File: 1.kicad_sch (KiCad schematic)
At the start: 32 parts, among them IC1 LTC4361IDC-2#TRMPBF, IC2 SI1470DH-T1-E3, IC3 SI1470DH-T1-E3, IC4 LTC4361IDC-2#TRMPBF, J1 Screw_Terminal_01x03, J2 Screw_Terminal_01x01, J3 Screw_Terminal_01x01, J4 ON2, J5 ON1, U1 LTC2990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

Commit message: Patch
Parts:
- removed IC1, IC4: LTC4361IDC-2#TRMPBF, SON45P200X200X80-9N-D, symbol LTC4361IDC-2#TRMPBF:LTC4361IDC-2#TRMPBF
- removed IC2, IC3: SI1470DH-T1-E3, SOT65P210X110-6N, symbol SI1470DH-T1-E3:SI1470DH-T1-E3
- removed J4: ON2, Connector_PinHeader_1.00mm:PinHeader_1x01_P1.00mm_Vertical, symbol Connector:Conn_01x01_Male
- removed J5: ON1, Connector_PinHeader_1.00mm:PinHeader_1x01_P1.00mm_Vertical, symbol Connector:Conn_01x01_Male
- removed R3, R4: 0.025, 0.025 ohm rst:CRA2512-FZ-R025ELF, symbol Device:R
- R5, R6, R7: value 60m -> 50m; footprint 60 mil rst:RESC7146X175N -> 50m RST:RESC3216X88N
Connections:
- net at R6.1, U2.1 (V1), U2.10 (VCC): now also Buck_IC1.4 (FB), C4.1, L2.2
- net at Boost_IC1.5 (VOUT), C2.2, D1.1 (K)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: now also R7.1, U3.1 (V1), U3.10 (VCC)
- no-connect marks 2 -> 0
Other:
- moved on the sheet: J1, R6, R7, SCLSDA1, SCLSDA2, U2, U3

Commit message: Fix
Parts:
- removed SHDN1: EN, Connector_PinHeader_1.00mm:PinHeader_1x02_P1.00mm_Vertical, symbol Connector:Conn_01x02_Male
- added R3: 1M, 1MEGA RST:RESC1608X55N, symbol Device:R
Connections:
- net at Boost_IC1.1 (SW), Buck_IC1.1 (VI), C1.1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: now also Buck_IC1.3 (EN)
- net at Boost_IC1.6 (VIN), D1.2 (A), L1.2: now also R3.2
- net at Boost_IC1.4 (~{SHDN}): now also R3.1
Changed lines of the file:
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@@
   (junction (at 129.54 83.82) (diameter 0) (color 0 0 0 0)
   )
+  (junction (at 110.49 110.49) (diameter 0) (color 0 0 0 0)
+  )
   (junction (at 162.56 120.65) (diameter 0) (color 0 0 0 0)
   )
@@
   (junction (at 162.56 125.73) (diameter 0) (color 0 0 0 0)
   )
+  (junction (at 76.2 83.82) (diameter 0) (color 0 0 0 0)
+  )
   (junction (at 162.56 33.02) (diameter 0) (color 0 0 0 0)
   )
@@
     (stroke (width 0) (type default) (color 0 0 0 0))
   )
+  (wire (pts (xy 110.49 110.49) (xy 110.49 105.41))
+    (stroke (width 0) (type default) (color 0 0 0 0))
+  )
   (wire (pts (xy 53.34 83.82) (xy 57.15 83.82))
     (stroke (width 0) (type default) (color 0 0 0 0))
@@
     (stroke (width 0) (type default) (color 0 0 0 0))
   )
-  (wire (pts (xy 53.34 109.22) (xy 53.34 105.41))
-    (stroke (width 0) (type default) (color 0 0 0 0))
-  )
   (wire (pts (xy 46.99 39.37) (xy 48.26 39.37))
     (stroke (width 0) (type default) (color 0 0 0 0))
@@
     (stroke (width 0) (type default) (color 0 0 0 0))
   )
+  (wire (pts (xy 76.2 83.82) (xy 76.2 100.33))
+    (stroke (width 0) (type default) (color 0 0 0 0))
+  )
   (wire (pts (xy 77.47 114.3) (xy 77.47 119.38))
     (stroke (width 0) (type default) (color 0 0 0 0))
@@
     (stroke (width 0) (type default) (color 0 0 0 0))
   )
+  (wire (pts (xy 116.84 118.11) (xy 116.84 110.49))
+    (stroke (width 0) (type default) (color 0 0 0 0))
+  )
   (wire (pts (xy 121.92 105.41) (xy 124.46 105.41))
     (stroke (width 0) (type default) (color 0 0 0 0))
   )
-  (wire (pts (xy 66.04 83.82) (xy 85.09 83.82))
+  (wire (pts (xy 66.04 83.82) (xy 76.2 83.82))
     (stroke (width 0) (type default) (color 0 0 0 0))
   )
@@
     (stroke (width 0) (type default) (color 0 0 0 0))
   )
-  (wire (pts (xy 53.34 100.33) (xy 53.34 102.87))
-    (stroke (width 0) (type default) (color 0 0 0 0))
-  )
   (wire (pts (xy 54.61 44.45) (xy 60.96 44.45))
     (stroke (width 0) (type default) (color 0 0 0 0))
@@
     (stroke (width 0) (type default) (color 0 0 0 0))
   )
+  (wire (pts (xy 76.2 83.82) (xy 85.09 83.82))
+    (stroke (width 0) (type default) (color 0 0 0 0))
+  )
   (wire (pts (xy 163.83 39.37) (xy 163.83 33.02))
     (stroke (width 0) (type default) (color 0 0 0 0))
@@
     (stroke (width 0) (type default) (color 0 0 0 0))
   )
-  (wire (pts (xy 110.49 111.76) (xy 110.49 105.41))
+  (wire (pts (xy 110.49 111.76) (xy 110.49 110.49))
     (stroke (width 0) (type default) (color 0 0 0 0))
   )
@@
     (stroke (width 0) (type default) (color 0 0 0 0))
   )
+  (wire (pts (xy 85.09 100.33) (xy 76.2 100.33))
+    (stroke (width 0) (type default) (color 0 0 0 0))
+  )
   (wire (pts (xy 194.31 125.73) (xy 170.18 125.73))
     (stroke (width 0) (type default) (color 0 0 0 0))
   )
-  (wire (pts (xy 53.34 100.33) (xy 85.09 100.33))
-    (stroke (width 0) (type default) (color 0 0 0 0))
-  )
   (wire (pts (xy 57.15 83.82) (xy 66.04 83.82))
     (stroke (width 0) (type default) (color 0 0 0 0))
   )
-  (wire (pts (xy 113.03 125.73) (xy 55.88 125.73))
-    (stroke (width 0) (type default) (color 0 0 0 0))
-  )
   (wire (pts (xy 194.31 100.33) (xy 200.66 100.33))
     (stroke (width 0) (type default) (color 0 0 0 0))
@@
     (stroke (width 0) (type default) (color 0 0 0 0))
   )
+  (wire (pts (xy 113.03 125.73) (xy 116.84 125.73))
+    (stroke (width 0) (type default) (color 0 0 0 0))
+  )
   (wire (pts (xy 161.29 67.31) (xy 161.29 69.85))
     (stroke (width 0) (type default) (color 0 0 0 0))
   )
+  (wire (pts (xy 116.84 110.49) (xy 110.49 110.49))
+    (stroke (width 0) (type default) (color 0 0 0 0))
+  )
   (wire (pts (xy 137.16 114.3) (xy 124.46 114.3))
     (stroke (width 0) (type default) (color 0 0 0 0))
@@
     (stroke (width 0) (type default) (color 0 0 0 0))
   )
-  (wire (pts (xy 55.88 125.73) (xy 55.88 109.22))
-    (stroke (width 0) (type default) (color 0 0 0 0))
-  )
   (wire (pts (xy 180.34 88.9) (xy 186.69 88.9))
     (stroke (width 0) (type default) (color 0 0 0 0))
@@
   )
   (wire (pts (xy 129.54 83.82) (xy 133.35 83.82))
-    (stroke (width 0) (type default) (color 0 0 0 0))
-  )
-  (wire (pts (xy 55.88 109.22) (xy 53.34 109.22))
     (stroke (width 0) (type default) (color 0 0 0 0))
   )
@@
     (pin "1")
   )
+  (symbol (lib_id "Device:R") (at 116.84 121.92 180) (unit 1)
+    (in_bom yes) (on_board yes) (fields_autoplaced)
+    (property "Reference" "R3" (id 0) (at 119.38 120.6499 0)
+      (effects (font (size 1.27 1.27)) (justify right))
+    )
+    (property "Value" "1M" (id 1) (at 119.38 123.1899 0)
+      (effects (font (size 1.27 1.27)) (justify right))
+    )
+    (property "Footprint" "1MEGA RST:RESC1608X55N" (id 2) (at 118.618 121.92 90)
+      (effects (font (size 1.27 1.27)) hide)
+    )
+    (property "Datasheet" "~" (id 3) (at 116.84 121.92 0)
+      (effects (font (size 1.27 1.27)) hide)
+    )
+    (pin "1")
+    (pin "2")
+  )
   (symbol (lib_id "power:Earth") (at 175.26 68.58 0) (unit 1)
     (in_bom yes) (on_board yes)
@@
     )
     (pin "1")
-  )
-  (symbol (lib_id "Connector:Conn_01x02_Male") (at 48.26 102.87 0) (unit 1)
-    (in_bom yes) (on_board yes)
-    (property "Reference" "SHDN1" (id 0) (at 43.18 105.41 0)
-      (effects (font (size 1.27 1.27) italic))
-    )
-    (property "Value" "EN" (id 1) (at 43.18 102.87 0)
-      (effects (font (size 1.27 1.27) italic))
-    )
-    (property "Footprint" "Connector_PinHeader_1.00mm:PinHeader_1x02_P1.00mm_Vertical" (id 2) (at 48.26 102.87 0)
-      (effects (font (size 1.27 1.27)) hide)
-    )
-    (property "Datasheet" "~" (id 3) (at 48.26 102.87 0)
-      (effects (font (size 1.27 1.27)) hide)
-    )
-    (pin "1")
-    (pin "2")
   )
   (symbol (lib_id "Device:R") (at 124.46 125.73 180) (unit 1)
@@
       (reference "R2") (unit 1) (value "30.9k") (footprint "rst 30.9k:RC0603FR-0730K9L")
     )
+    (path "/9a83f5dd-a9a9-4595-818a-33edb0a4e5ba"
+      (reference "R3") (unit 1) (value "1M") (footprint "1MEGA RST:RESC1608X55N")
+    )
     (path "/ff683999-9a0b-4b2c-b7a1-8133c85893b8"
       (reference "R5") (unit 1) (value "50m") (footprint "50m RST:RESC3216X88N")
@@
       (reference "SCLSDA3") (unit 1) (value "EN") (footprint "Connector_PinHeader_1.00mm:PinHeader_1x02_P1.00mm_Vertical")
     )
-    (path "/c2af6cd7-8992-4aad-8e85-60f76aaf6747"
-      (reference "SHDN1") (unit 1) (value "EN") (footprint "Connector_PinHeader_1.00mm:PinHeader_1x02_P1.00mm_Vertical")
-    )
     (path "/0b256487-9344-4785-bb3c-397bc7af7b0d"

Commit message: Replaced Al elec caps
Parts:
- C1, C4: footprint capa 10uf:CAPAE530X610N -> 10uF MLCC:CAPC2012X94N
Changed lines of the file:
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@@
       (effects (font (size 1.27 1.27)) (justify left))
     )
-    (property "Footprint" "capa 10uf:CAPAE530X610N" (id 2) (at 67.31 119.38 0)
+    (property "Footprint" "10uF MLCC:CAPC2012X94N" (id 2) (at 67.31 119.38 0)
       (effects (font (size 1.27 1.27)) (justify left) hide)
     )
@@
       (effects (font (size 1.27 1.27)) (justify left))
     )
-    (property "Footprint" "capa 10uf:CAPAE530X610N" (id 2) (at 134.62 93.98 0)
+    (property "Footprint" "10uF MLCC:CAPC2012X94N" (id 2) (at 134.62 93.98 0)
       (effects (font (size 1.27 1.27)) (justify left) hide)
     )
@@
     )
     (path "/ceccba2c-fd35-4027-b469-b5251bf9371d"
-      (reference "C1") (unit 1) (value "10uF") (footprint "capa 10uf:CAPAE530X610N")
+      (reference "C1") (unit 1) (value "10uF") (footprint "10uF MLCC:CAPC2012X94N")
     )
     (path "/58050e2e-2661-4a39-9c6f-f880badad60f"
@@
     )
     (path "/e5d3408d-c91a-46dd-a8ed-70976bafd174"
-      (reference "C4") (unit 1) (value "10uF") (footprint "capa 10uf:CAPAE530X610N")
+      (reference "C4") (unit 1) (value "10uF") (footprint "10uF MLCC:CAPC2012X94N")
     )
     (path "/408b0048-2750-407d-ab86-a1e2f34d0c4c"

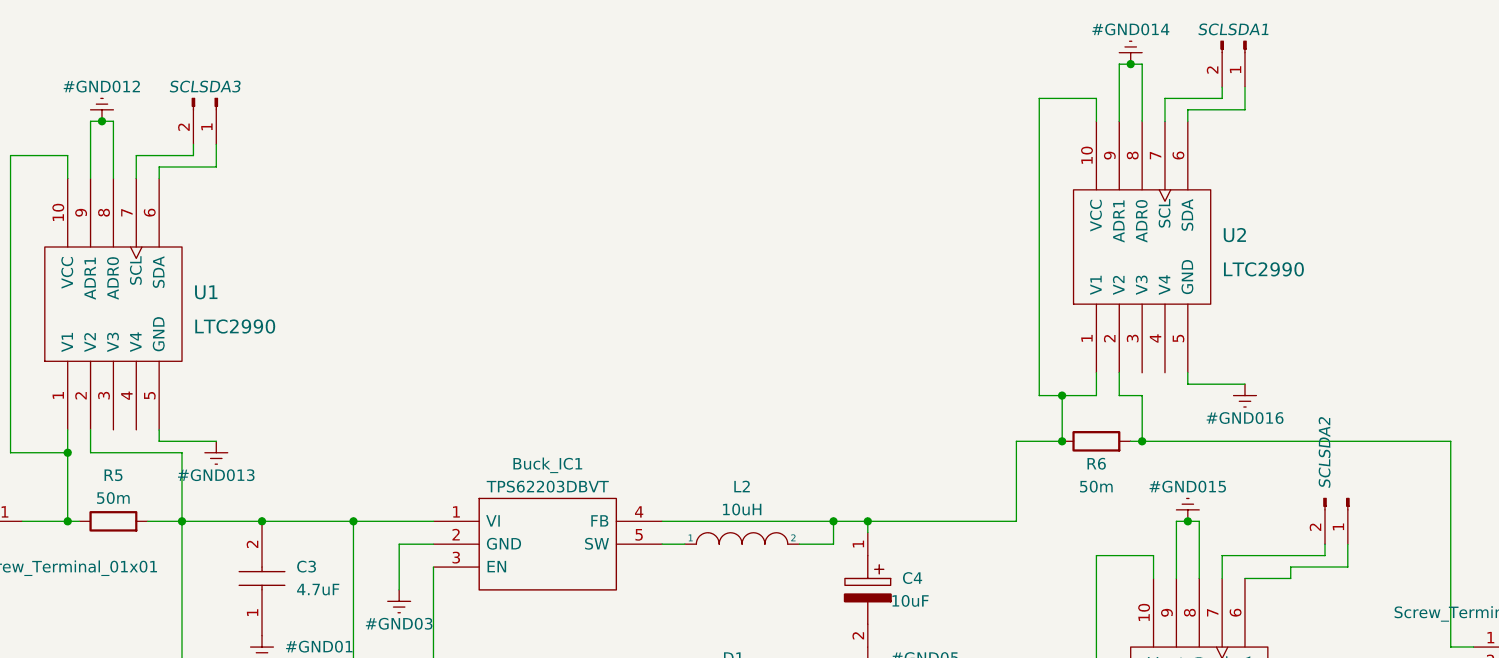
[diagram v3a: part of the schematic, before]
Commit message: Fixed routing issues and naming of pins
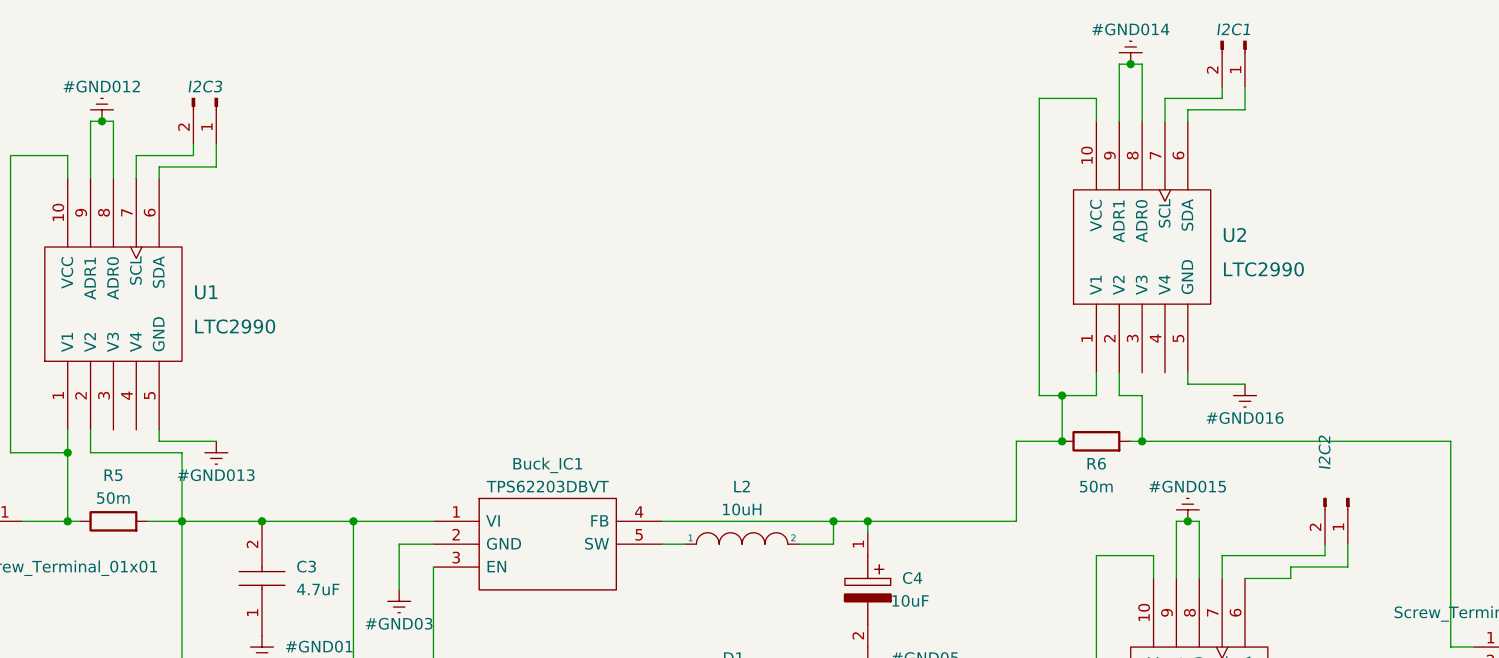
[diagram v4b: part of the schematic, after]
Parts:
- renumbered SCLSDA1 to I2C1, SCLSDA2 to I2C2, SCLSDA3 to I2C3
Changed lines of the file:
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@@
   (symbol (lib_id "Connector:Conn_01x02_Male") (at 175.26 30.48 270) (unit 1)
     (in_bom yes) (on_board yes)
-    (property "Reference" "SCLSDA1" (id 0) (at 173.99 29.21 90)
+    (property "Reference" "I2C1" (id 0) (at 173.99 29.21 90)
       (effects (font (size 1.27 1.27) italic))
     )
@@
   (symbol (lib_id "Connector:Conn_01x02_Male") (at 186.69 81.28 270) (unit 1)
     (in_bom yes) (on_board yes)
-    (property "Reference" "SCLSDA2" (id 0) (at 184.15 76.2 0)
+    (property "Reference" "I2C2" (id 0) (at 184.15 76.2 0)
       (effects (font (size 1.27 1.27) italic))
     )
@@
   (symbol (lib_id "Connector:Conn_01x02_Male") (at 60.96 36.83 270) (unit 1)
     (in_bom yes) (on_board yes)
-    (property "Reference" "SCLSDA3" (id 0) (at 59.69 35.56 90)
+    (property "Reference" "I2C3" (id 0) (at 59.69 35.56 90)
       (effects (font (size 1.27 1.27) italic))
     )
@@
       (reference "D1") (unit 1) (value "D_Schottky") (footprint "Schottky dd:DIOM5026X220N")
     )
+    (path "/51b12217-3f6f-4523-ba9c-90af2efcba7f"
+      (reference "I2C1") (unit 1) (value "EN") (footprint "Connector_PinHeader_1.00mm:PinHeader_1x02_P1.00mm_Vertical")
+    )
+    (path "/cced1236-94c4-4406-ae7a-7e694e456057"
+      (reference "I2C2") (unit 1) (value "EN") (footprint "Connector_PinHeader_1.00mm:PinHeader_1x02_P1.00mm_Vertical")
+    )
+    (path "/da964c11-8316-4be6-83b3-ae1c8d0e8293"
+      (reference "I2C3") (unit 1) (value "EN") (footprint "Connector_PinHeader_1.00mm:PinHeader_1x02_P1.00mm_Vertical")
+    )
     (path "/28059cb1-6349-43cb-8aef-aa43fbccf280"
       (reference "J1") (unit 1) (value "Screw_Terminal_01x03") (footprint "TerminalBlock_MetzConnect:TerminalBlock_MetzConnect_Type055_RT01503HDWU_1x03_P5.00mm_Horizontal")
@@
       (reference "R7") (unit 1) (value "50m") (footprint "50m RST:RESC3216X88N")
     )
-    (path "/51b12217-3f6f-4523-ba9c-90af2efcba7f"
-      (reference "SCLSDA1") (unit 1) (value "EN") (footprint "Connector_PinHeader_1.00mm:PinHeader_1x02_P1.00mm_Vertical")
-    )
-    (path "/cced1236-94c4-4406-ae7a-7e694e456057"
-      (reference "SCLSDA2") (unit 1) (value "EN") (footprint "Connector_PinHeader_1.00mm:PinHeader_1x02_P1.00mm_Vertical")
-    )
-    (path "/da964c11-8316-4be6-83b3-ae1c8d0e8293"
-      (reference "SCLSDA3") (unit 1) (value "EN") (footprint "Connector_PinHeader_1.00mm:PinHeader_1x02_P1.00mm_Vertical")
-    )
     (path "/0b256487-9344-4785-bb3c-397bc7af7b0d"

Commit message: FInal...I guess
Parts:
- D1: footprint Schottky dd:DIOM5026X220N -> Schottky DD with stock:DIOM5126X265N
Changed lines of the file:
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@@
     (property "Reference" "D1" (id 0) (at 118.4275 99.06 0))
     (property "Value" "D_Schottky" (id 1) (at 118.4275 101.6 0))
-    (property "Footprint" "Schottky dd:DIOM5026X220N" (id 2) (at 118.11 105.41 0)
+    (property "Footprint" "Schottky DD with stock:DIOM5126X265N" (id 2) (at 118.11 105.41 0)
       (effects (font (size 1.27 1.27)) hide)
     )
@@
     )
     (path "/408b0048-2750-407d-ab86-a1e2f34d0c4c"
-      (reference "D1") (unit 1) (value "D_Schottky") (footprint "Schottky dd:DIOM5026X220N")
+      (reference "D1") (unit 1) (value "D_Schottky") (footprint "Schottky DD with stock:DIOM5126X265N")
     )
     (path "/51b12217-3f6f-4523-ba9c-90af2efcba7f"

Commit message: sch edits
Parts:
- D1: value D_Schottky -> STPS2150A
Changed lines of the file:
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@@
     (in_bom yes) (on_board yes)
     (property "Reference" "D1" (id 0) (at 118.4275 99.06 0))
-    (property "Value" "D_Schottky" (id 1) (at 118.4275 101.6 0))
+    (property "Value" "STPS2150A" (id 1) (at 118.4275 101.6 0))
     (property "Footprint" "Schottky DD with stock:DIOM5126X265N" (id 2) (at 118.11 105.41 0)
       (effects (font (size 1.27 1.27)) hide)
@@
     )
     (path "/408b0048-2750-407d-ab86-a1e2f34d0c4c"
-      (reference "D1") (unit 1) (value "D_Schottky") (footprint "Schottky DD with stock:DIOM5126X265N")
+      (reference "D1") (unit 1) (value "STPS2150A") (footprint "Schottky DD with stock:DIOM5126X265N")
     )
     (path "/51b12217-3f6f-4523-ba9c-90af2efcba7f"
